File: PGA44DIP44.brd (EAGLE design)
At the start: 58.4 x 20.3 mm, 9 parts, among them CN1 JTAG, IC1 LM2937ET-3.3/NOPB

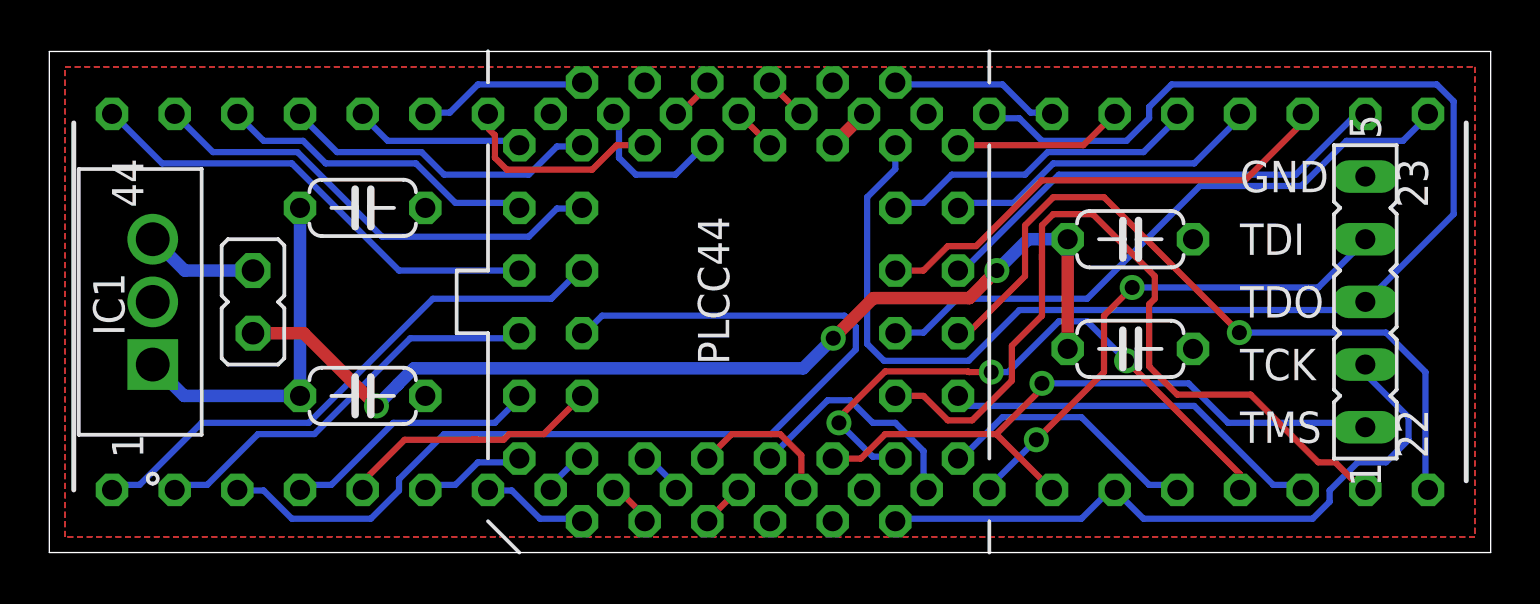
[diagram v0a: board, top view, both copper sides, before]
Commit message: Fixed XC9572 version.
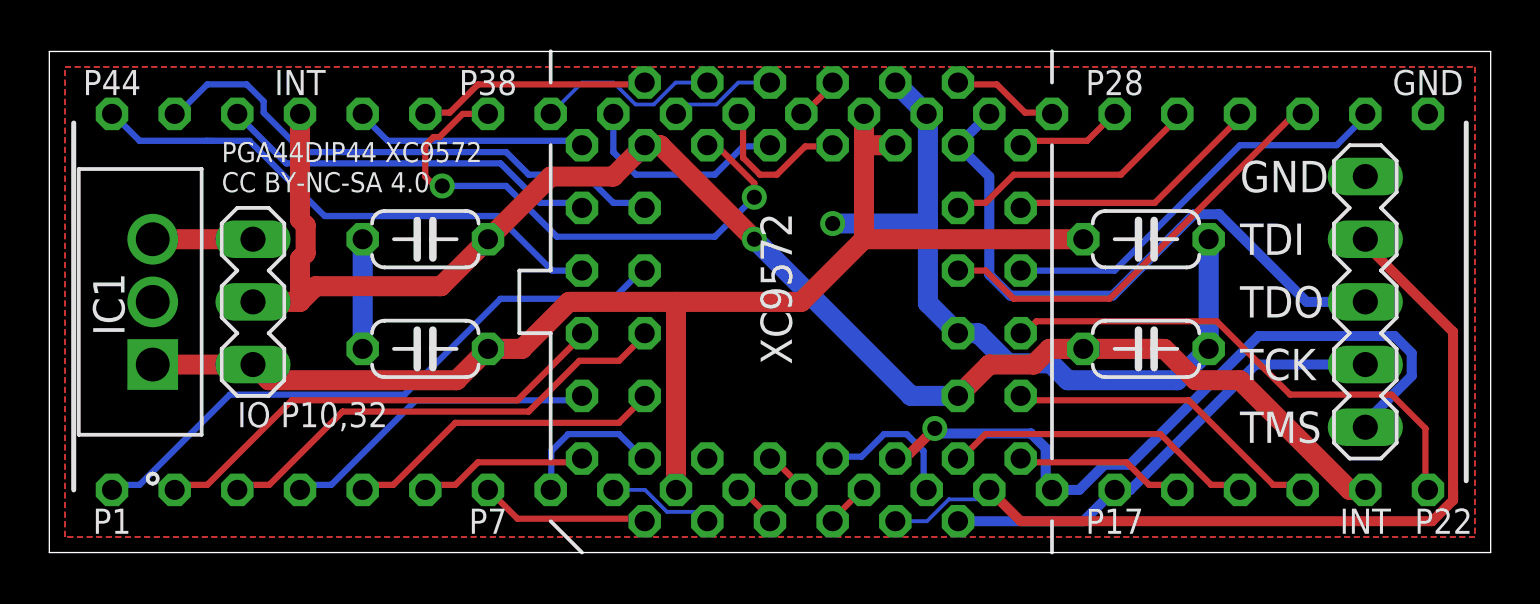
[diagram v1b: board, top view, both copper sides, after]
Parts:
- removed PLCC44: PGA44, PGA44DIP44:PGA44
- added XC9572: PGA44, PGA44DIP44:PGA44
- CN1: device con-lsta:FE05-1 -> PGA44DIP44:MA05-1
- DIP44: value DIP44 -> (none)
- JP1: value (none) -> PCONF; device PGA44DIP44:JP1 -> PGA44DIP44:MA03-1
- moved C2 31.8 mm to (44.5, 12.7)
- moved C4 28.6 mm to (15.2, 12.7), turned to 180 degrees
- moved C1 3.18 mm to (15.2, 8.26), turned to 180 degrees
- moved C3 0.64 mm to (44.5, 8.26)
- turned JP1 to 90 degrees
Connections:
- removed net L10: DIP44.10, PLCC44.10
- removed net L15: CN1.4, DIP44.15, PLCC44.15
- removed net L16: CN1.1, DIP44.16, PLCC44.16
- removed net L17: CN1.2, DIP44.17, PLCC44.17
- removed net L21: DIP44.21, PLCC44.21
- removed net L23: DIP44.23, PLCC44.23
- removed net L30: CN1.3, DIP44.30, PLCC44.30
- removed net L31: DIP44.31, PLCC44.31
- removed net L32: DIP44.32, PLCC44.32
- removed net L41: DIP44.41, PLCC44.41
- removed net N$1: IC1.3, JP1.1
- new net TCK: CN1.2, DIP44.17, XC9572.17
- new net TDI: CN1.4, DIP44.15, XC9572.15
- new net TDO: CN1.3, DIP44.30, XC9572.30
- new net TMS: CN1.1, DIP44.16, XC9572.16
- new net V33: IC1.3, JP1.3
- net GND: now also DIP44.23, DIP44.31, XC9572.10, XC9572.23, XC9572.31
- net L1: now also XC9572.1; no longer PLCC44.1
- net L11: now also XC9572.11; no longer PLCC44.11
- net L12: now also XC9572.12; no longer PLCC44.12
- net L13: now also XC9572.13; no longer PLCC44.13
- net L14: now also XC9572.14; no longer PLCC44.14
- net L18: now also XC9572.18; no longer PLCC44.18
- net L19: now also XC9572.19; no longer PLCC44.19
- net L2: now also XC9572.2; no longer PLCC44.2
- net L20: now also XC9572.20; no longer PLCC44.20
- net L22: now also XC9572.22; no longer PLCC44.22
- net L24: now also XC9572.24; no longer PLCC44.24
- net L25: now also XC9572.25; no longer PLCC44.25
- net L26: now also XC9572.26; no longer PLCC44.26
- net L27: now also XC9572.27; no longer PLCC44.27
- net L28: now also XC9572.28; no longer PLCC44.28
- net L29: now also XC9572.29; no longer PLCC44.29
- net L3: now also XC9572.3; no longer PLCC44.3
- net L33: now also XC9572.33; no longer PLCC44.33
- net L34: now also XC9572.34; no longer PLCC44.34
- net L35: now also XC9572.35; no longer PLCC44.35
- net L36: now also XC9572.36; no longer PLCC44.36
- net L37: now also XC9572.37; no longer PLCC44.37
- net L38: now also XC9572.38; no longer PLCC44.38
- net L39: now also XC9572.39; no longer PLCC44.39
- net L4: now also XC9572.4; no longer PLCC44.4
- net L40: now also XC9572.40; no longer PLCC44.40
- net L42: now also XC9572.42; no longer PLCC44.42
- net L43: now also XC9572.43; no longer PLCC44.43
- net L44: now also XC9572.44; no longer PLCC44.44
- net L5: now also XC9572.5; no longer PLCC44.5
- net L6: now also XC9572.6; no longer PLCC44.6
- net L7: now also XC9572.7; no longer PLCC44.7
- net L8: now also XC9572.8; no longer PLCC44.8
- net L9: now also XC9572.9; no longer PLCC44.9
- net VCCINT: now also DIP44.21, DIP44.41, XC9572.21, XC9572.41
- net VCCIO: now also DIP44.10, DIP44.32, JP1.1, XC9572.32
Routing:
- net L30: track 60.4 -> 0.00 mm
- net VCCIO: track 14.1 -> 54.3 mm
- net TDI: track 0.00 -> 36.5 mm
- net GND: track 0.00 -> 35.2 mm, vias 0 -> 1
- net L21: track 33.2 -> 0.00 mm
- net TMS: track 0.00 -> 30.0 mm, vias 0 -> 1
- net L17: track 27.3 -> 0.00 mm
- net L16: track 27.1 -> 0.00 mm, vias 1 -> 0
- net TDO: track 0.00 -> 26.0 mm
- net L23: track 25.3 -> 0.00 mm
- net L3: track 41.1 -> 19.2 mm
- net VCCINT: track 41.5 -> 62.9 mm, vias 3 -> 1
- net L15: track 20.9 -> 0.00 mm, vias 2 -> 0
- net TCK: track 0.00 -> 19.1 mm
- net L38: track 8.56 -> 22.5 mm, vias 0 -> 2
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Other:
- board text added: "INT"
- board text added: "IO P10,32"
- board text added: "P1"
- board text added: "P17"
- board text added: "P22"
- board text added: "P28"
- board text added: "P38"
- board text added: "P44"
- board text added: "P7"
- board text added: "PGA44DIP44 XC9572 CC BY-NC-SA 4.0"
